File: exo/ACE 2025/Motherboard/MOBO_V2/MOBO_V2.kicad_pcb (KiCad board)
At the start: 4 copper layers, 100 x 100 mm, 82 parts, among them J301 USB_C_UART, J302 USB_C_DEBUG, J601 Conn_02x10_Counter_Clockwise, J602 Micro_SD_Card, J701 DOS RJ45, J702 DROITE RJ45, J703 GAUCHE RJ45, Q201 AO3401A, U201 AP7361C-33E, U202 TPS562242DRLR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

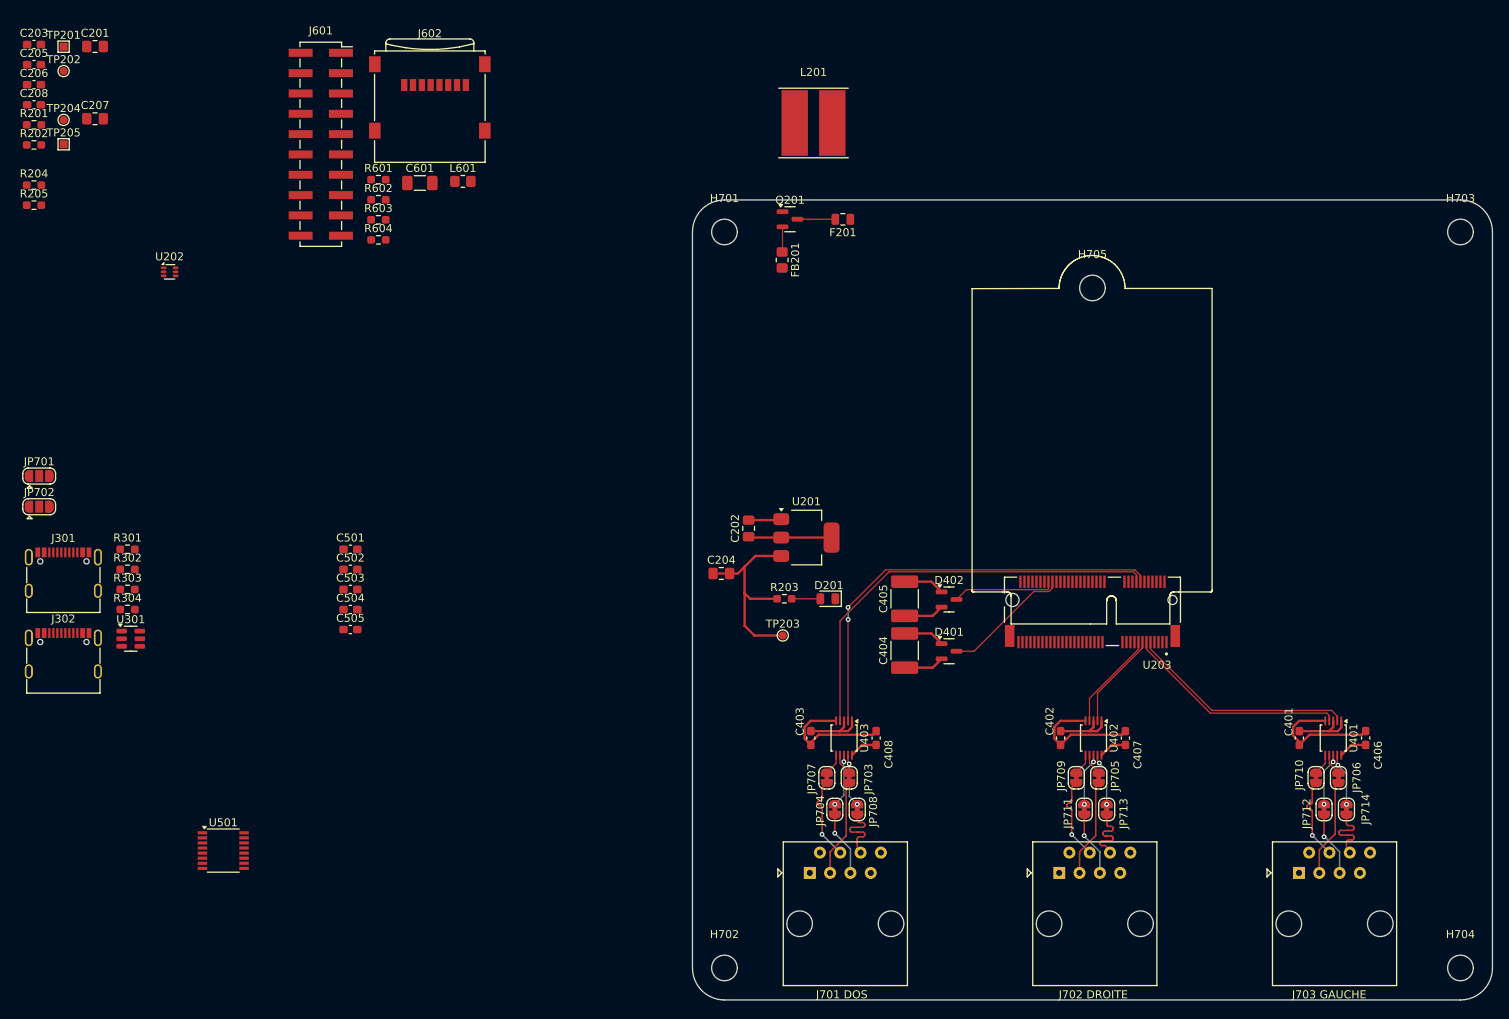
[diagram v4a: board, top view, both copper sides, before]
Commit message: ajout du uSD,USBC et du connecteur
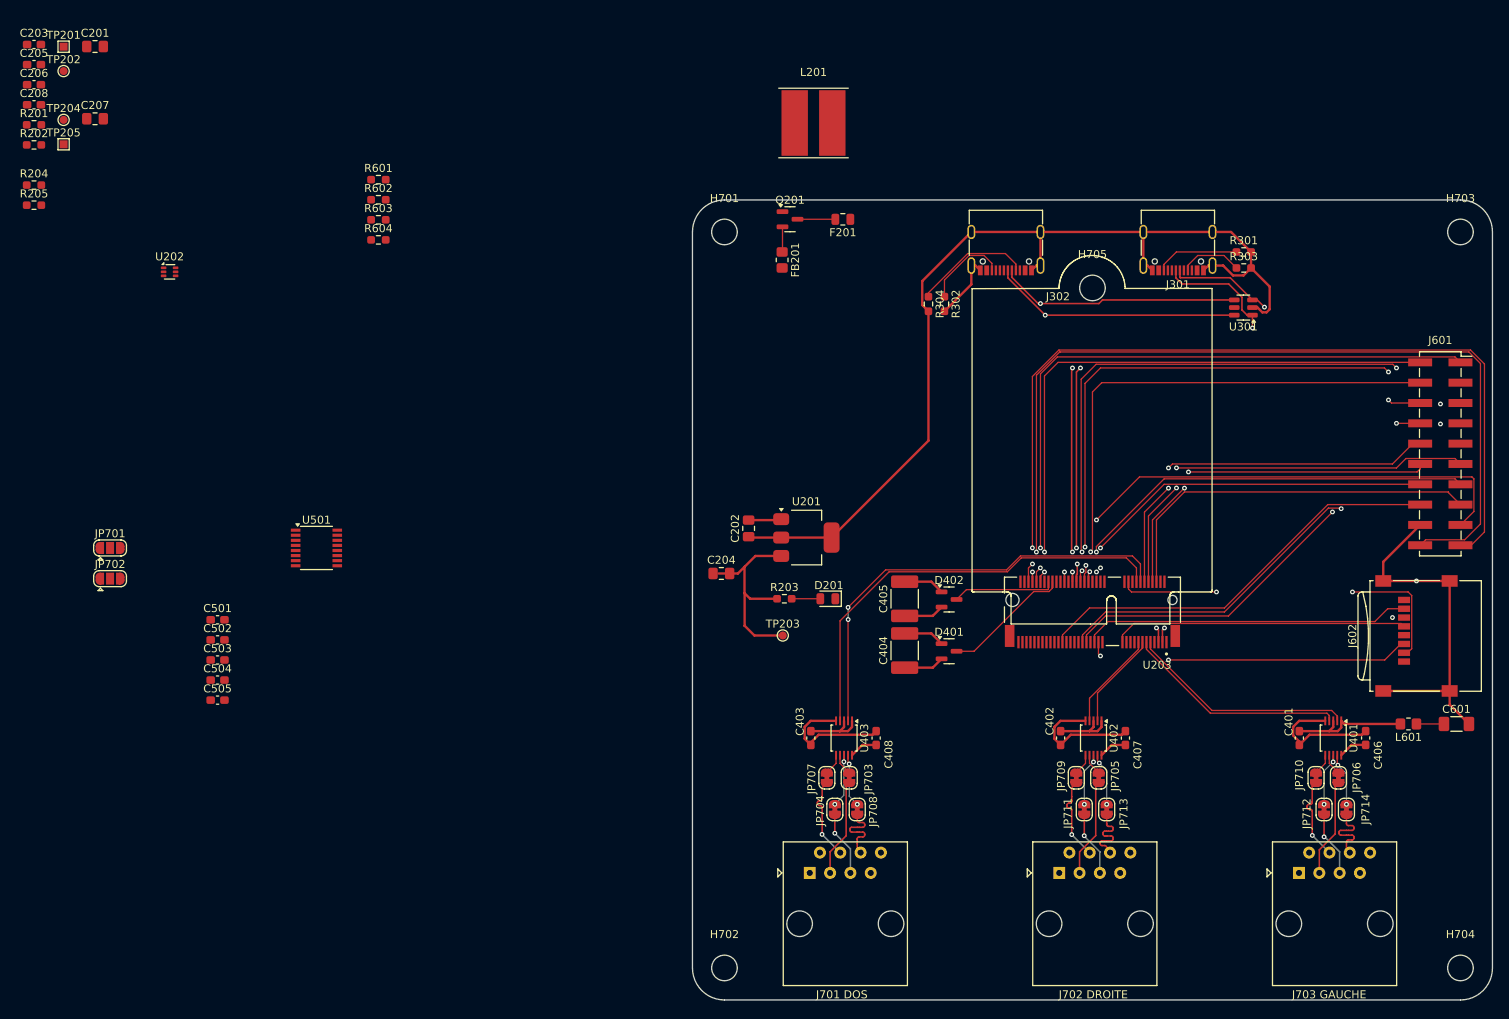
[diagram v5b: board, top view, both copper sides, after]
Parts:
- moved C601 146.2 mm to (198.5, 105.5)
- moved J301 145.7 mm to (163.7, 45.1), turned to 180 degrees
- moved R303 145.2 mm to (171.9, 48.5)
- moved J601 145.2 mm to (196.5, 71.7)
- moved U301 145.1 mm to (171.9, 53.5), turned to 180 degrees
- moved R301 144.4 mm to (171.9, 46.5)
- moved J602 140.5 mm to (193.5, 94.5), turned to 90 degrees
- moved L601 136.3 mm to (192.5, 105.5), turned to 180 degrees
- moved J302 129.1 mm to (142.2, 45.1), turned to 180 degrees
- moved R302 107.4 mm to (134.5, 53.0), turned to -90 degrees
- moved R304 107.2 mm to (132.5, 53.0), turned to -90 degrees
- moved U501 39.6 mm to (56.0, 83.5)
- moved C501 18.8 mm to (43.6, 92.5)
- moved C504 18.8 mm to (43.6, 100.0)
- moved C502 18.8 mm to (43.6, 95.0)
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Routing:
- net GND: track 68.1 -> 237.7 mm, vias 0 -> 2
- net /ESP32_SD_EXTRA/PWM_3: track 0.00 -> 112.1 mm, vias 0 -> 2
- net /ESP32_SD_EXTRA/PWM_4: track 0.00 -> 109.2 mm, vias 0 -> 2
- net /ESP32_SD_EXTRA/PWM_2: track 0.00 -> 79.9 mm, vias 0 -> 2
- net /ESP32_SD_EXTRA/GPIO34: track 0.00 -> 75.8 mm, vias 0 -> 4
- net /ESP32_SD_EXTRA/PWM_1: track 0.00 -> 73.6 mm, vias 0 -> 2
- net /ESP32_SD_EXTRA/GPIO26: track 0.00 -> 71.5 mm, vias 0 -> 4
- net /USB/DEBUG_D-: track 0.00 -> 67.3 mm, vias 0 -> 4
- net /USB/DEBUG_D+: track 0.00 -> 66.3 mm, vias 0 -> 4
- net /ESP32_SD_EXTRA/GPIO15: track 0.00 -> 65.4 mm, vias 0 -> 2
- net /ESP32_SD_EXTRA/GPIO45: track 0.00 -> 65.3 mm, vias 0 -> 2
- net /USB/FT231_D+: track 0.00 -> 60.1 mm, vias 0 -> 2
- net /USB/FT231_D-: track 0.00 -> 59.3 mm, vias 0 -> 2
- net /ESP32_SD_EXTRA/GPIO16: track 0.00 -> 57.1 mm, vias 0 -> 2
- net /ESP32_SD_EXTRA/GPIO33: track 0.00 -> 56.6 mm, vias 0 -> 2
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
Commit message: Alimentaation quasi fini
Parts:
- moved C208 111.5 mm to (126.6, 63.0)
- moved TP204 109.8 mm to (125.2, 73.4)
- moved C206 107.3 mm to (118.7, 69.3), turned to 180 degrees
- moved R204 106.1 mm to (120.8, 73.4), turned to 180 degrees
- moved C207 102.4 mm to (126.8, 57.9)
- moved R205 101.2 mm to (116.5, 73.4), turned to 180 degrees
- moved R201 97.7 mm to (112.3, 64.5), turned to 180 degrees
- moved C203 97.4 mm to (109.9, 59.9), turned to 180 degrees
- moved C205 96.5 mm to (105.4, 69.2), turned to -90 degrees
- moved TP205 96.0 mm to (111.5, 73.4)
- moved TP202 94.1 mm to (114.2, 52.0)
- moved R202 91.7 mm to (106.9, 64.5), turned to 180 degrees
- moved C201 88.6 mm to (109.9, 55.4), turned to 180 degrees
- moved TP201 86.8 mm to (105.4, 52.0)
- moved R601 85.1 mm to (71.9, 122.1)
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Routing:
- net Vcc_5V: track 14.8 -> 42.2 mm
- net VIN_PROTECTION: track 0.00 -> 23.8 mm
- net Net-(U202-SW): track 0.00 -> 18.0 mm, vias 0 -> 3
- net Net-(U202-VFB): track 0.00 -> 15.1 mm
- net Net-(U202-EN): track 0.00 -> 9.11 mm, vias 0 -> 2
- net GND: track 237.7 -> 244.6 mm
- net Net-(U202-VBST): track 0.00 -> 3.40 mm

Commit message: Quelque détail
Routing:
- net VBUS: track 0.00 -> 61.0 mm, vias 0 -> 7

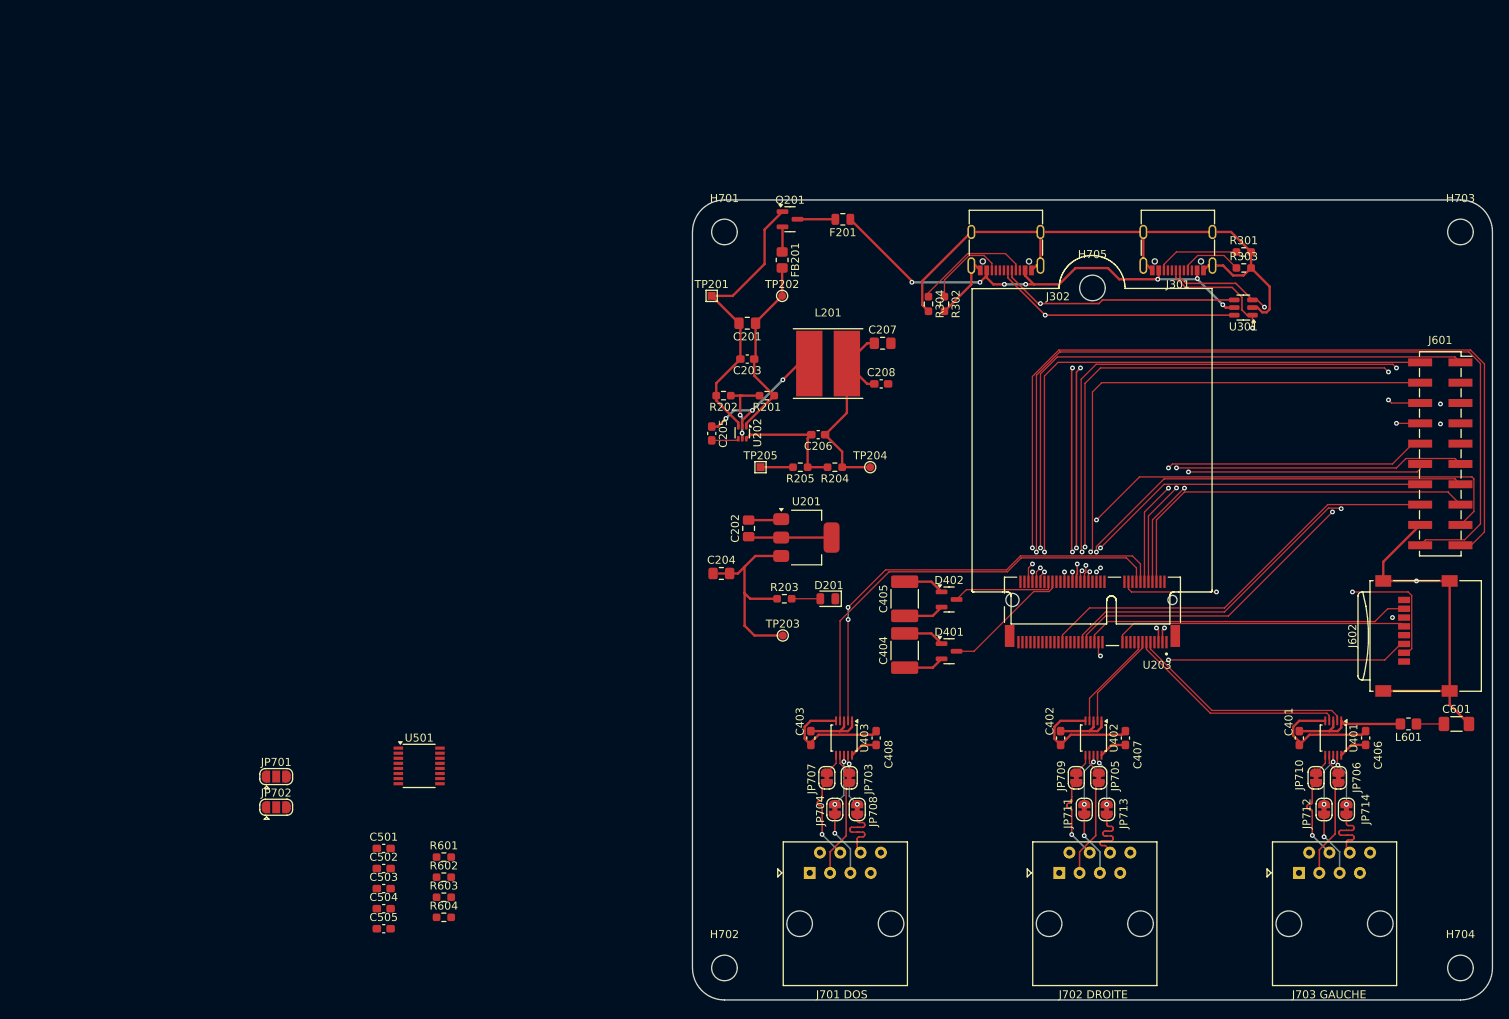
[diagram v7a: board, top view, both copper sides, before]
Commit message: ajout CAN
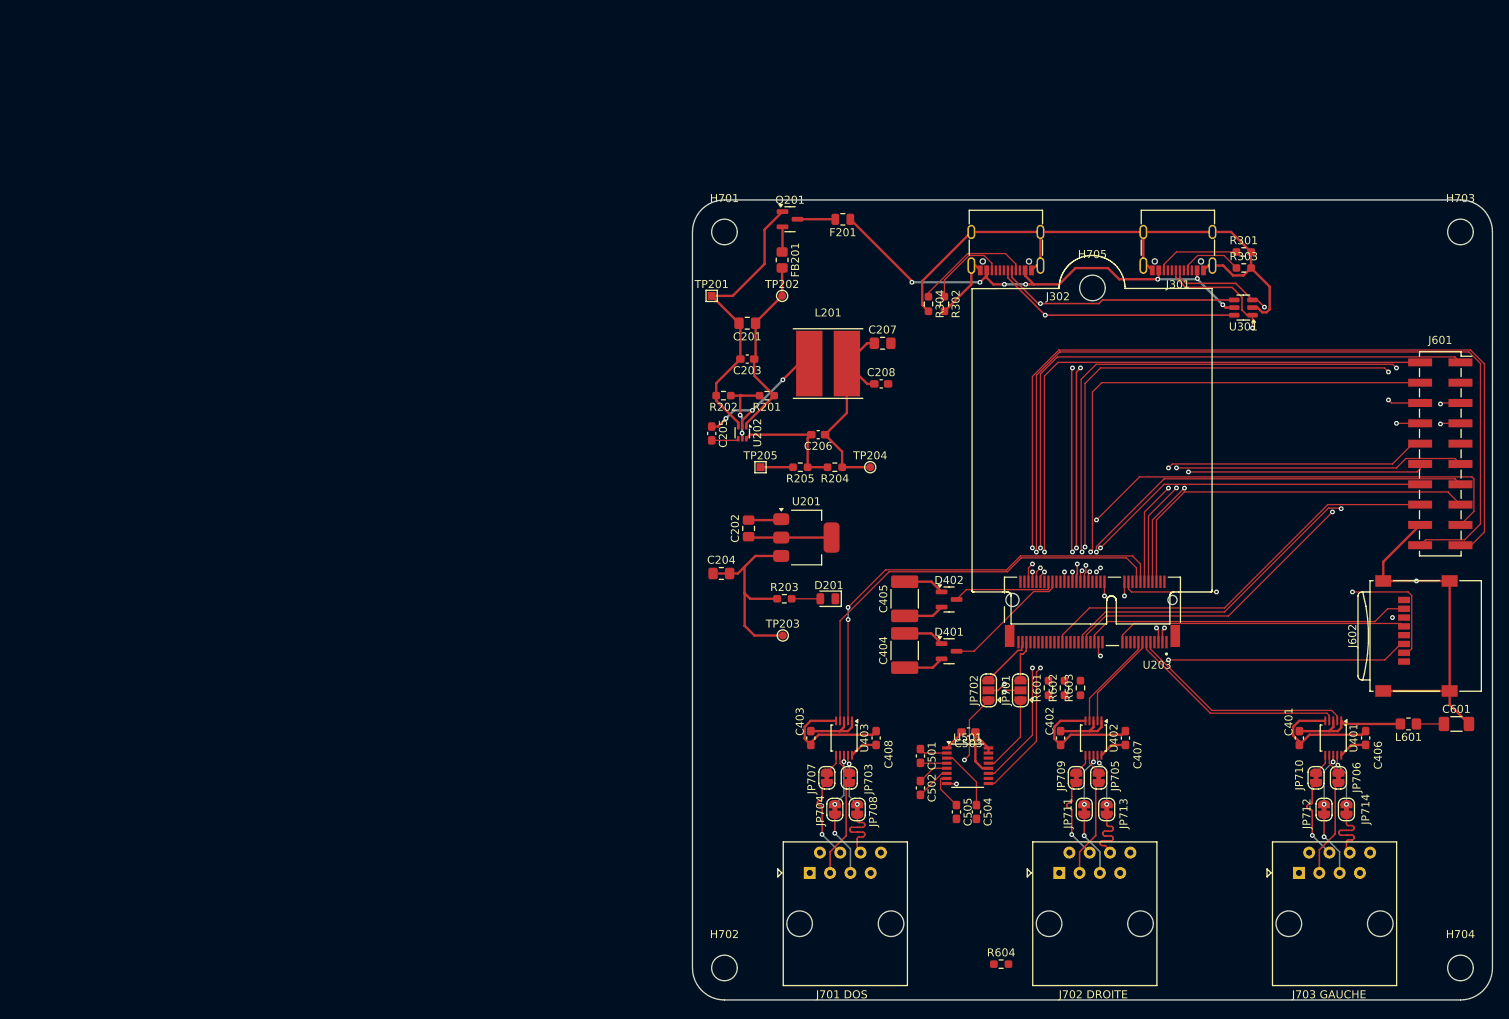
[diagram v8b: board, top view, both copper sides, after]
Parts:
- moved JP701 93.7 mm to (144.0, 101.3), turned to 90 degrees
- moved JP702 90.2 mm to (140.0, 101.3), turned to 90 degrees
- moved R603 83.8 mm to (151.5, 101.0), turned to 90 degrees
- moved R602 81.1 mm to (149.5, 101.0), turned to 90 degrees
- moved R601 78.5 mm to (147.5, 101.0), turned to 90 degrees
- moved C503 75.7 mm to (137.5, 106.5), turned to 180 degrees
- moved C504 75.1 mm to (138.5, 116.5), turned to -90 degrees
- moved C505 73.1 mm to (136.0, 116.5), turned to -90 degrees
- moved R604 69.9 mm to (141.6, 135.5)
- moved U501 68.6 mm to (137.4, 110.7)
- moved C501 68.1 mm to (131.5, 109.5), turned to -90 degrees
- moved C502 67.8 mm to (131.5, 113.5), turned to -90 degrees
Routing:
- net /CAN/GPIO18_U1_RXD: track 0.00 -> 33.6 mm, vias 0 -> 2
- net /CAN/GPIO17_U1_TXD: track 0.00 -> 30.4 mm, vias 0 -> 2
- net /Connecteurs/CAN+: track 0.00 -> 27.5 mm, vias 0 -> 1
- net /Connecteurs/CAN-: track 0.00 -> 27.4 mm, vias 0 -> 1
- net /CAN/RS232_RX: track 0.00 -> 13.3 mm, vias 0 -> 2
- net /CAN/RS232_TX: track 0.00 -> 9.88 mm
- net Vcc_3V3: track 66.5 -> 75.4 mm
- net Net-(U501-V+): track 0.00 -> 7.82 mm
- net /CAN/CAN_N: track 0.00 -> 6.77 mm
- net /CAN/CAN_P: track 0.00 -> 5.23 mm
- net Net-(U501-V-): track 0.00 -> 4.89 mm
- net Net-(U501-C2-): track 0.00 -> 4.41 mm
- net Net-(U501-C2+): track 0.00 -> 3.96 mm
- net Net-(U501-C1+): track 0.00 -> 3.51 mm
- net Net-(U501-C1-): track 0.00 -> 3.32 mm
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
